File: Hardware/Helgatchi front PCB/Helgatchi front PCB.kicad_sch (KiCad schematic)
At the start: 27 parts, among them J1 Battery, J3 SPI Screen, M1 MOTOR, Q1 NMOS, Q2 NMOS, SW1 SW_LEFT, SW2 SW_CENTER, SW3 SW_RIGHT, U1 XIAO-ESP32-S3-SMD

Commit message: R2
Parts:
- removed H3, H4: M2, MountingHole:MountingHole_2.2mm_M2_Pad, symbol Mechanical:MountingHole_Pad
- removed J3: SPI Screen, 0.96 inch OLED:Untitled, symbol Connector_Generic:Conn_01x07
- added C3: 100nF, Capacitor_SMD:C_0603_1608Metric, symbol Device:C_Small
- added C7: 10uF, Capacitor_SMD:C_0603_1608Metric, symbol Device:C_Small
- added D4: WS2812C, WS2812B 2020:LED_WS2812B-2020_PLCC4_2.0x2.0mm, symbol LED:WS2812B
- added J2: SCREEN, Connector_Molex:Molex_PicoBlade_53261-0871_1x08-1MP_P1.25mm_Horizontal, symbol Connector_Generic_MountingPin:Conn_01x08_MountingPin
- added J3: SMA, Connector_Coaxial:SMA_Samtec_SMA-J-P-H-ST-EM1_EdgeMount, symbol Connector:Conn_Coaxial
- added J4: u.FL, Connector_Coaxial:U.FL_Molex_MCRF_73412-0110_Vertical, symbol Connector:Conn_Coaxial
- added JP1: LEDs, Jumper:SolderJumper-3_P1.3mm_Open_RoundedPad1.0x1.5mm_NumberLabels, symbol Jumper:SolderJumper_3_Open
- BZ1, R2: now not fitted; now left out of the parts list
- C1, C2, C4, C5, C6: LCSC Part # (none) -> C14663
- D1: footprint Diode_SMD:D_1206_3216Metric_Pad1.42x1.75mm_HandSolder -> Diode_SMD:D_0603_1608Metric; LCSC Part # (none) -> C35621074
- D2, D3, D5, D6, D7: value WS2812B -> WS2812C; footprint LED_SMD:LED_WS2812B-2020_PLCC4_2.0x2.0mm -> WS2812B 2020:LED_WS2812B-2020_PLCC4_2.0x2.0mm; LCSC Part # (none) -> C42417600
- H1, H2: footprint MountingHole:MountingHole_2.2mm_M2_Pad -> Mounting_Wuerth:Mounting_Wuerth_WA-SMSI-M2_H8mm_9774080243; now in the parts list
- J1: value Battery -> BATTERY; symbol Connector_Generic:Conn_01x02 -> Connector_Generic_MountingPin:Conn_01x02_MountingPin; LCSC Part # (none) -> C160402
- Q1: LCSC Part # (none) -> C20917
- Q2: LCSC Part # (none) -> C20917; now not fitted; now left out of the parts list
- SW1: value SW_LEFT -> LEFT BUTTON
- SW2: value SW_CENTER -> CENTER BUTTON
- SW3: value SW_RIGHT -> RIGHT BUTTON
- U1: value XIAO-ESP32-S3-SMD -> XIAO ESP32-S3; now not fitted; now left out of the parts list
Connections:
- net +3.3V: now also J2.8 (Pin_8), JP1.1 (A)
- net +BATT: now also J1.2 (Pin_2), JP1.3 (B); no longer C1.2, C2.2, C4.2, C5.2, C6.2, D2.1 (VDD), D3.1 (VDD), D5.1 (VDD), D6.1 (VDD), D7.1 (VDD), J1.1 (Pin_1)
- net -BATT: now also J1.1 (Pin_1); no longer J1.2 (Pin_2)
- net BUZZER: no longer U1.3 (GPIO3_A2_D2)
- net GND: now also J1.MP (MountPin), C3.1, C7.2, D4.3 (VSS), J2.7 (Pin_7), J2.MP (MountPin), J3.2 (Ext), J4.2 (Ext)
- net SPI_CS: now also J2.4 (Pin_4)
- net SPI_DC: now also J2.3 (Pin_3)
- net SPI_MOSI: now also J2.6 (Pin_6)
- net SPI_RES: now also J2.2 (Pin_2)
- net SPI_SCK: now also J2.5 (Pin_5)
- net at D5.4 (DIN): now also D4.2 (DOUT); no longer D3.2 (DOUT)
- new net: D3.2 (DOUT), D4.4 (DIN)
- new net: J3.1 (In), J4.1 (In)
- new net LED_PWR: C1.2, C2.2, C3.2, C4.2, C5.2, C6.2, C7.1, D2.1 (VDD), D3.1 (VDD), D4.1 (VDD), D5.1 (VDD), D6.1 (VDD), D7.1 (VDD), JP1.2 (C)
- new net SPI_BL: J2.1 (Pin_1), U1.3 (GPIO3_A2_D2)
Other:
- note added: "Notes * properly place mounting holes for front and back board * breakup front and back * update/validate laser cutter files * add SMA and u.FL connectors * https://jlcpcb.com/partdetail/DreamLNK-SMA_KEP901/C914556 * https://jlcpcb.com/partdetail/HJTech-HJSMA501/C2693812"
- note removed: "Notes * Determine screen pinout * Break out 3rd/4th button * Standoffs? * Add buzzer * Add haptics * Add buttons"
- moved on the sheet: D1, M1, Q1, R1

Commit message: slopsoftware
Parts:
- removed J3: SMA, Connector_Coaxial:SMA_Samtec_SMA-J-P-H-ST-EM1_EdgeMount, symbol Connector:Conn_Coaxial
- removed J4: u.FL, Connector_Coaxial:U.FL_Molex_MCRF_73412-0110_Vertical, symbol Connector:Conn_Coaxial

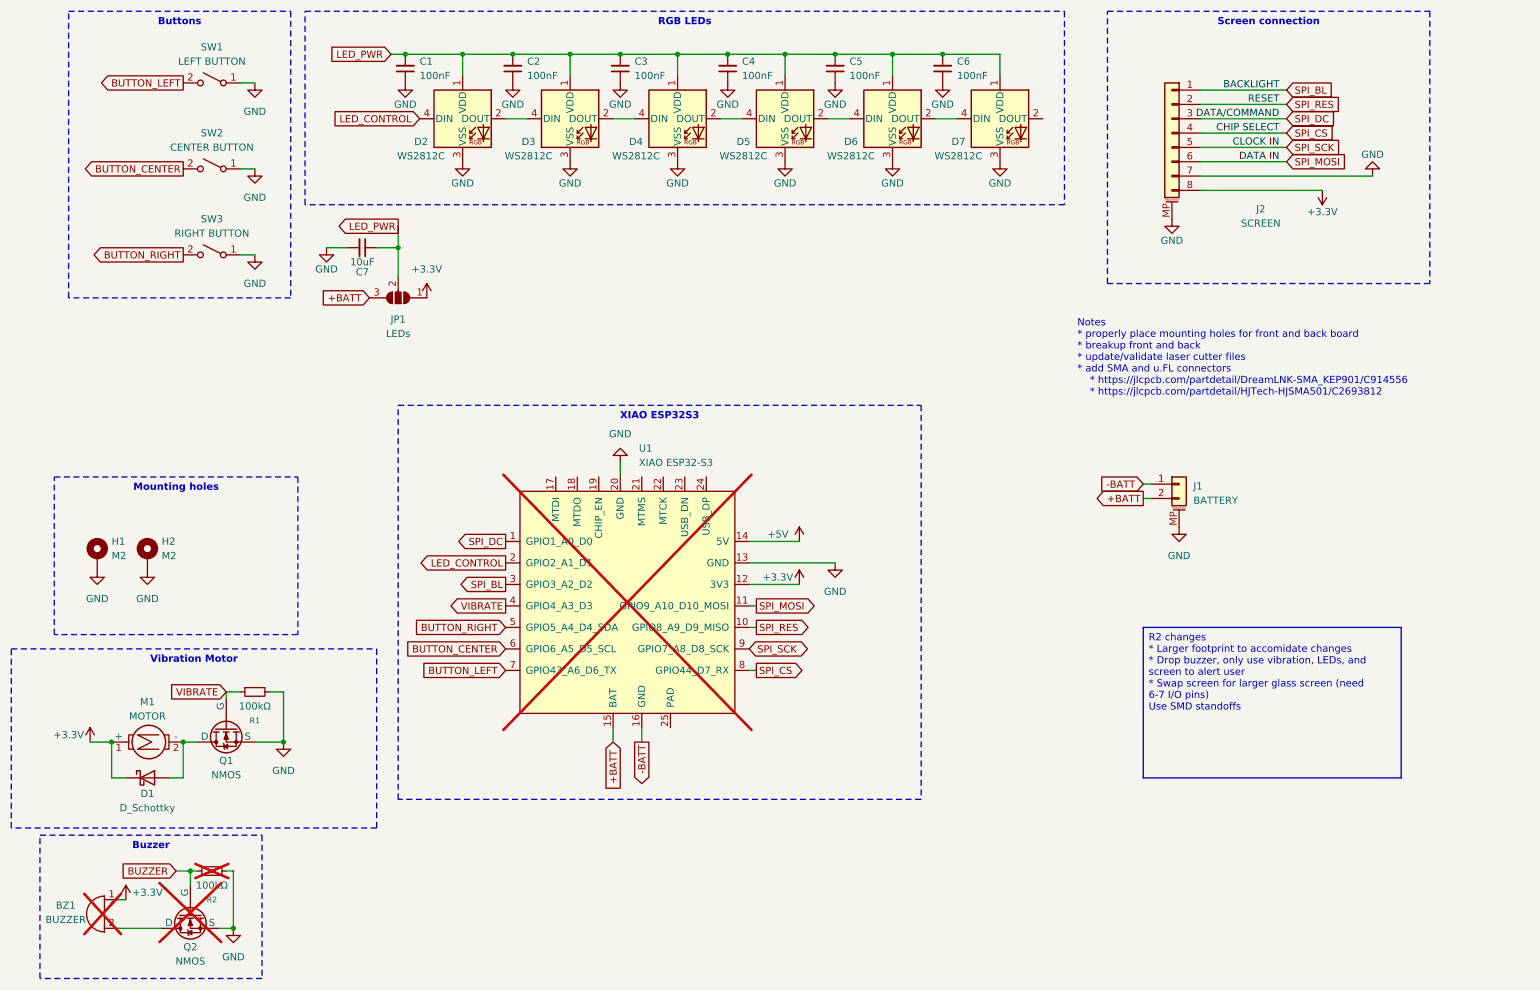
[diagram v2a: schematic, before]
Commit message: Swap to WS2812B-4020-H2 Footprint variant
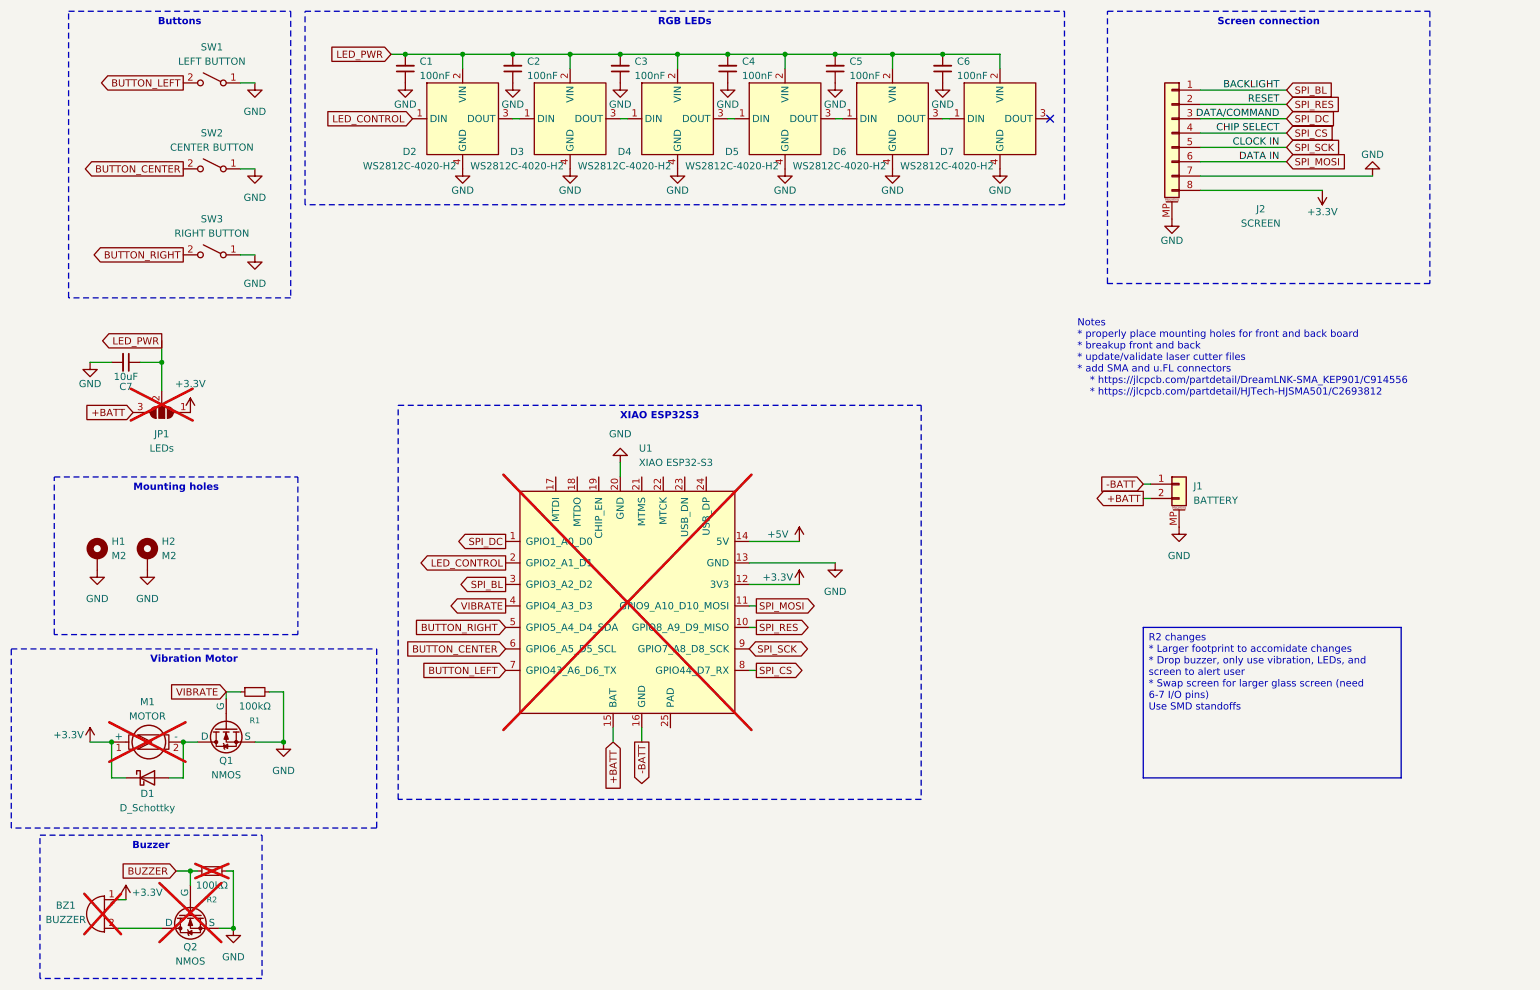
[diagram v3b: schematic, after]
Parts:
- D2, D3, D4, D5, D6, D7: value WS2812C -> WS2812C-4020-H2; footprint WS2812B 2020:LED_WS2812B-2020_PLCC4_2.0x2.0mm -> WS2812:WS2812C-4020-H2; symbol LED:WS2812B -> WS2812:WS2812B-4020; LCSC Part # C42417600 -> C42417604
- H1, H2: now left out of the parts list
- JP1: now not fitted
- M1: now not fitted; now left out of the parts list
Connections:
- net GND: now also D2.4 (GND), D3.4 (GND), D4.4 (GND), D5.4 (GND), D6.4 (GND), D7.4 (GND), Q1.2 (S); no longer D2.3 (VSS), D3.3 (VSS), D4.3 (VSS), D5.3 (VSS), D6.3 (VSS), D7.3 (VSS), Q1.3 (S)
- net LED_CONTROL: now also D2.1 (DIN); no longer D2.4 (DIN)
- net LED_PWR: now also D2.2 (VIN), D3.2 (VIN), D4.2 (VIN), D5.2 (VIN), D6.2 (VIN), D7.2 (VIN); no longer D2.1 (VDD), D3.1 (VDD), D4.1 (VDD), D5.1 (VDD), D6.1 (VDD), D7.1 (VDD)
- net VIBRATE: now also Q1.1 (G); no longer Q1.2 (G)
- net at D1.2 (A), M1.2 (-): now also Q1.3 (D); no longer Q1.1 (D)
- new net: D6.3 (DOUT), D7.1 (DIN)
- new net: D3.3 (DOUT), D4.1 (DIN)
- new net: D4.3 (DOUT), D5.1 (DIN)
- new net: D5.3 (DOUT), D6.1 (DIN)
- new net: D2.3 (DOUT), D3.1 (DIN)
- no-connect marks 0 -> 1
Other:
- moved on the sheet: C7

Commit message: Back PCB changes
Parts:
- J2: LCSC Part # C293349 -> C7433459
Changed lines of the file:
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@@
 			)
 		)
-		(property "LCSC Part #" "C293349"
+		(property "LCSC Part #" "C7433459"
 			(at 223.52 36.83 0)
 			(effects

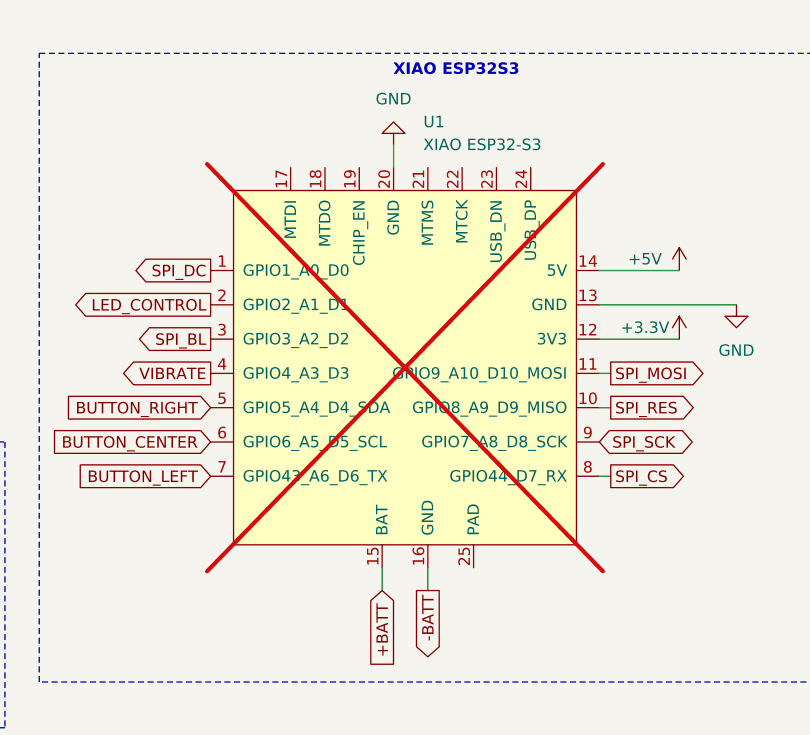
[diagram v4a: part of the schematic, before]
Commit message: LCSC part # changes
- Changed MOLEX Picoblate part number out for generic picoblade
- Added part number and adjusted DNP for ESP32-S3
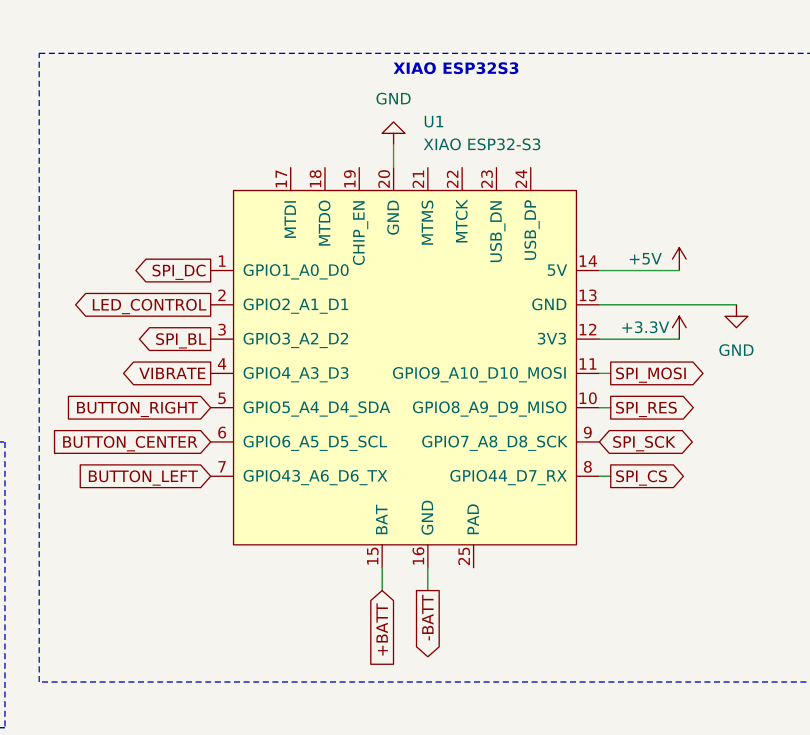
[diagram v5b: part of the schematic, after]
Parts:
- U1: LCSC Part # (none) -> C9900124959; now fitted; now in the parts list
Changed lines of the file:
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@@
 		(unit 1)
 		(exclude_from_sim no)
-		(in_bom no)
+		(in_bom yes)
 		(on_board yes)
-		(dnp yes)
+		(dnp no)
 		(property "Reference" "U1"
 			(at 129.032 92.71 0)
@@
 			)
 		)
-		(property "LCSC Part #" ""
+		(property "LCSC Part #" "C9900124959"
 			(at 127 120.65 0)
 			(effects

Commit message: Helgatchi front PCB: update to R2.5
Bump PCB revision to R2.5 and apply small layout/text tweaks: adjust gr_text position, update render_cache label/date, add font thickness to silkscreen effects, and shift numerous silkscreen/graphics coordinates. Also update corresponding schematic and netlist, and add production archives (Helgatchi_Front_R2.4.zip and a backups zip).
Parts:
- D1: footprint Diode_SMD:D_0603_1608Metric -> SDM2U30CSP:SDM2U30CSP
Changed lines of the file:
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@@
 			)
 		)
-		(property "Footprint" "Diode_SMD:D_0603_1608Metric"
+		(property "Footprint" "SDM2U30CSP:SDM2U30CSP"
 			(at 41.91 151.13 0)
 			(effects
